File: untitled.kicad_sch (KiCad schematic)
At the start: 32 parts

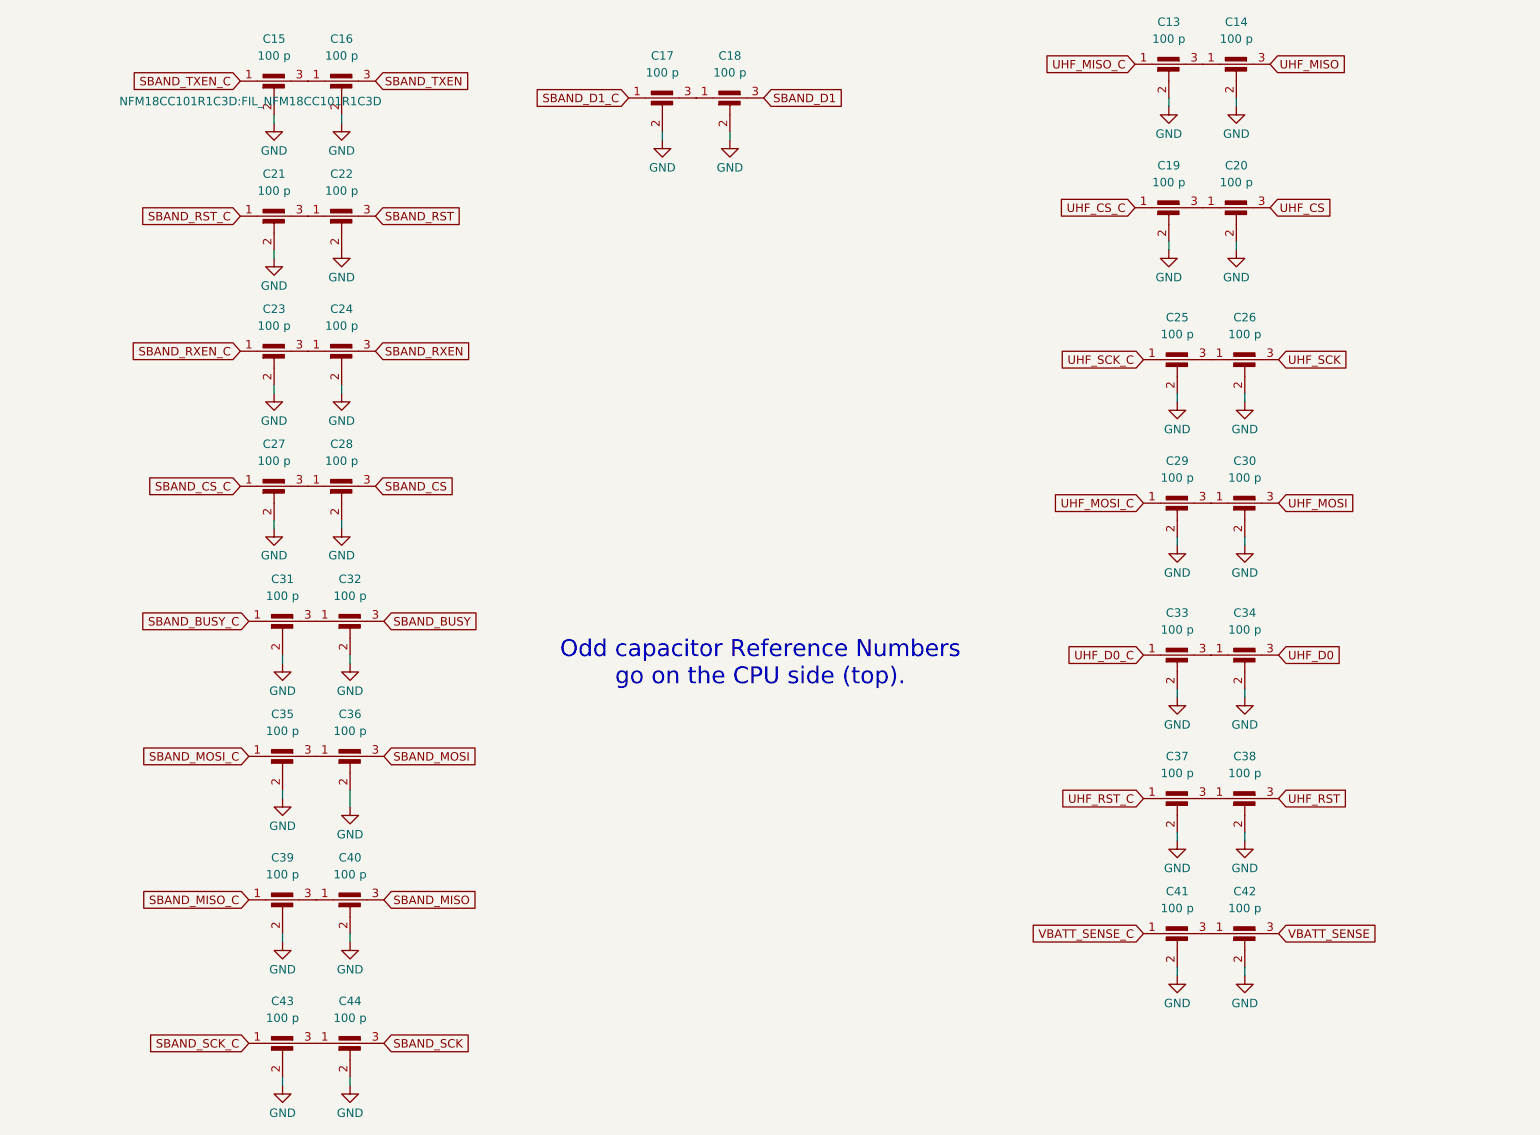
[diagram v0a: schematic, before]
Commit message: started placement of feed through
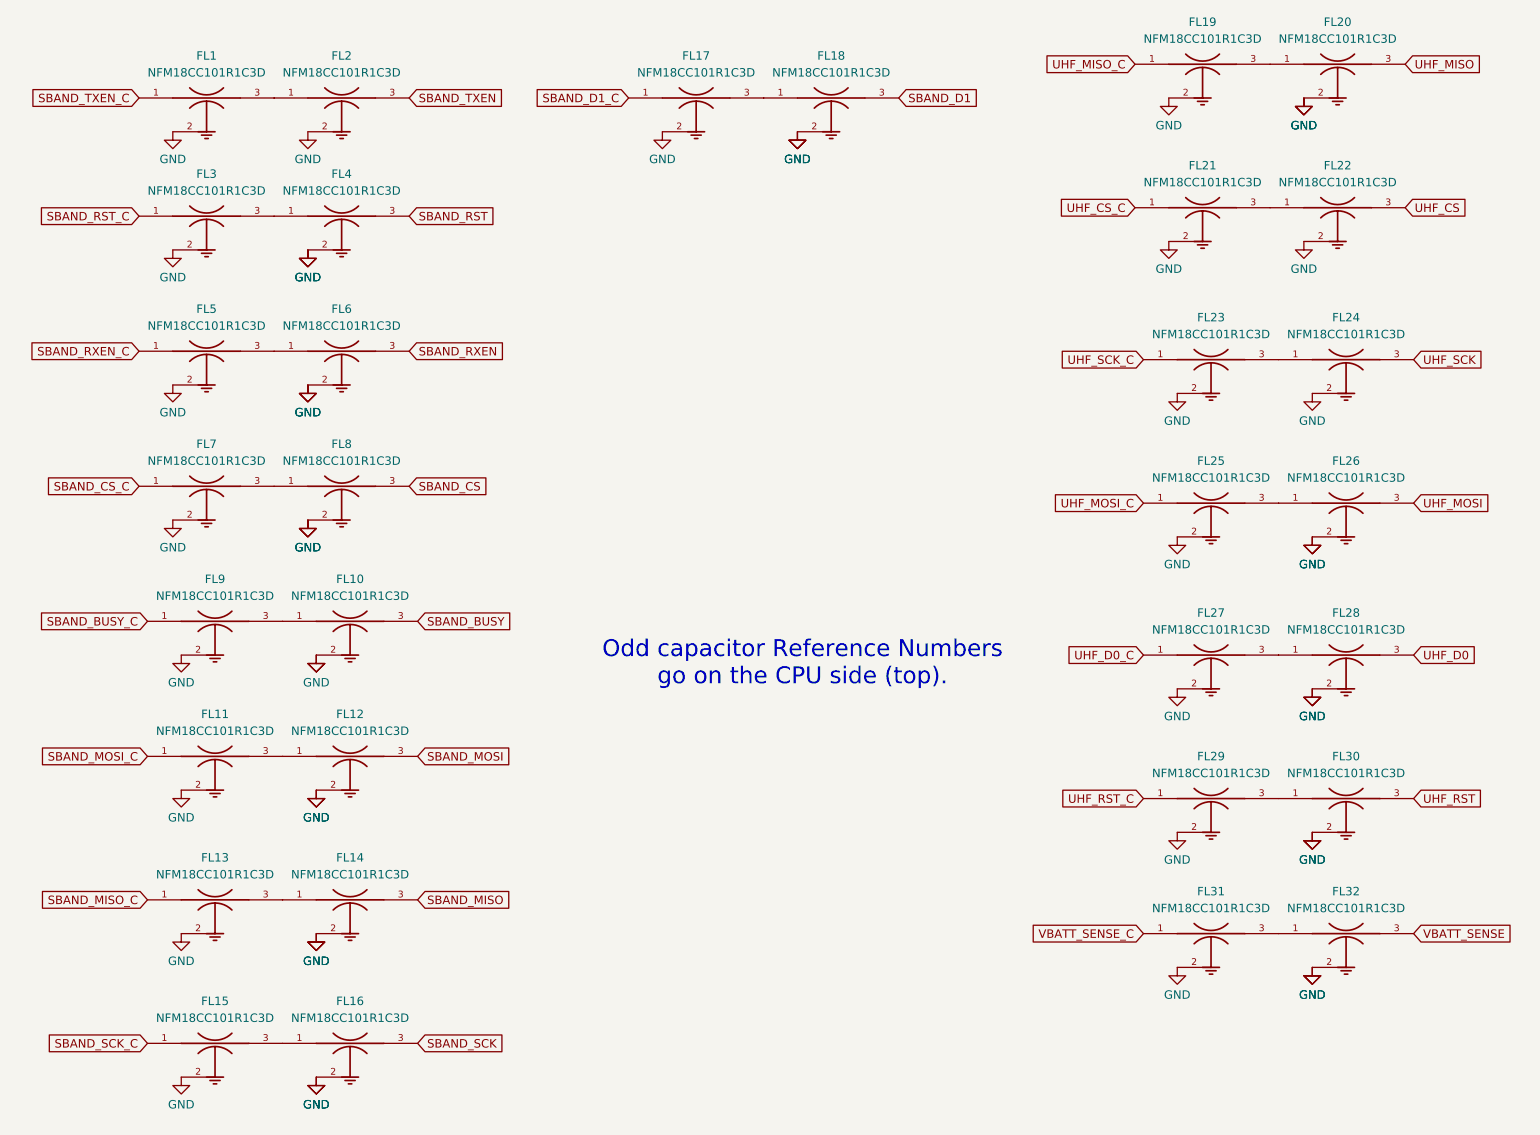
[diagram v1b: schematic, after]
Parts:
- removed C13, C14, C15, C16, C17, C18, C19, C20, C21, C22, C23, C24, C25, C26, C27, C28, C29, C30, C31, C32, C33, C34, C35, C36, C37, C38, C39, C40, C41, C42, C43, C44: 100 p, NFM18CC101R1C3D:FIL_NFM18CC101R1C3D, symbol Device:C_Feedthrough
- added FL1, FL10, FL11, FL12, FL13, FL14, FL15, FL16, FL17, FL18, FL19, FL2, FL20, FL21, FL22, FL23, FL24, FL25, FL26, FL27, FL28, FL29, FL3, FL30, FL31, FL32, FL4, FL5, FL6, FL7, FL8, FL9: NFM18CC101R1C3D, NFM18CC101R1C3D:FIL_NFM18CC101R1C3D, symbol NFM18CC101R1C3D:NFM18CC101R1C3D
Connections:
- net GND: now also FL1.2, FL1.2_1, FL1.2_2, FL1.2_3, FL1.2_4, FL10.2, FL10.2_1, FL10.2_2, FL10.2_3, FL10.2_4, FL11.2, FL11.2_1, FL11.2_2, FL11.2_3, FL11.2_4, FL12.2, FL12.2_1, FL12.2_2, FL12.2_3, FL12.2_4, FL13.2, FL13.2_1, FL13.2_2, FL13.2_3, FL13.2_4, FL14.2, FL14.2_1, FL14.2_2, FL14.2_3, FL14.2_4, FL15.2, FL15.2_1, FL15.2_2, FL15.2_3, FL15.2_4, FL16.2, FL16.2_1, FL16.2_2, FL16.2_3, FL16.2_4, FL17.2, FL17.2_1, FL17.2_2, FL17.2_3, FL17.2_4, FL18.2, FL18.2_1, FL18.2_2, FL18.2_3, FL18.2_4, FL19.2, FL19.2_1, FL19.2_2, FL19.2_3, FL19.2_4, FL2.2, FL2.2_1, FL2.2_2, FL2.2_3, FL2.2_4, FL20.2, FL20.2_1, FL20.2_2, FL20.2_3, FL20.2_4, FL21.2, FL21.2_1, FL21.2_2, FL21.2_3, FL21.2_4, FL22.2, FL22.2_1, FL22.2_2, FL22.2_3, FL22.2_4, FL23.2, FL23.2_1, FL23.2_2, FL23.2_3, FL23.2_4, FL24.2, FL24.2_1, FL24.2_2, FL24.2_3, FL24.2_4, FL25.2, FL25.2_1, FL25.2_2, FL25.2_3, FL25.2_4, FL26.2, FL26.2_1, FL26.2_2, FL26.2_3, FL26.2_4, FL27.2, FL27.2_1, FL27.2_2, FL27.2_3, FL27.2_4, FL28.2, FL28.2_1, FL28.2_2, FL28.2_3, FL28.2_4, FL29.2, FL29.2_1, FL29.2_2, FL29.2_3, FL29.2_4, FL3.2, FL3.2_1, FL3.2_2, FL3.2_3, FL3.2_4, FL30.2, FL30.2_1, FL30.2_2, FL30.2_3, FL30.2_4, FL31.2, FL31.2_1, FL31.2_2, FL31.2_3, FL31.2_4, FL32.2, FL32.2_1, FL32.2_2, FL32.2_3, FL32.2_4, FL4.2, FL4.2_1, FL4.2_2, FL4.2_3, FL4.2_4, FL5.2, FL5.2_1, FL5.2_2, FL5.2_3, FL5.2_4, FL6.2, FL6.2_1, FL6.2_2, FL6.2_3, FL6.2_4, FL7.2, FL7.2_1, FL7.2_2, FL7.2_3, FL7.2_4, FL8.2, FL8.2_1, FL8.2_2, FL8.2_3, FL8.2_4, FL9.2, FL9.2_1, FL9.2_2, FL9.2_3, FL9.2_4
- net SBAND_BUSY: now also FL10.3
- net SBAND_BUSY_C: now also FL9.1
- net SBAND_CS: now also FL8.3
- net SBAND_CS_C: now also FL7.1
- net SBAND_D1: now also FL18.3
- net SBAND_D1_C: now also FL17.1
- net SBAND_MISO: now also FL14.3
- net SBAND_MISO_C: now also FL13.1
- net SBAND_MOSI: now also FL12.3
- net SBAND_MOSI_C: now also FL11.1
- net SBAND_RST: now also FL4.3
- net SBAND_RST_C: now also FL3.1
- net SBAND_RXEN: now also FL6.3
- net SBAND_RXEN_C: now also FL5.1
- net SBAND_SCK: now also FL16.3
- net SBAND_SCK_C: now also FL15.1
- net SBAND_TXEN: now also FL2.3
- net SBAND_TXEN_C: now also FL1.1
- net UHF_CS: now also FL22.3
- net UHF_CS_C: now also FL21.1
- net UHF_D0: now also FL28.3
- net UHF_D0_C: now also FL27.1
- net UHF_MISO: now also FL20.3
- net UHF_MISO_C: now also FL19.1
- net UHF_MOSI: now also FL26.3
- net UHF_MOSI_C: now also FL25.1
- net UHF_RST: now also FL30.3
- net UHF_RST_C: now also FL29.1
- net UHF_SCK: now also FL24.3
- net UHF_SCK_C: now also FL23.1
- net VBATT_SENSE: now also FL32.3
- net VBATT_SENSE_C: now also FL31.1
- new net: FL19.3, FL20.1
- new net: FL27.3, FL28.1
- new net: FL25.3, FL26.1
- new net: FL21.3, FL22.1
- new net: FL5.3, FL6.1
- new net: FL7.3, FL8.1
- new net: FL23.3, FL24.1
- new net: FL10.1, FL9.3
- new net: FL1.3, FL2.1
- new net: FL15.3, FL16.1
- new net: FL3.3, FL4.1
- new net: FL17.3, FL18.1
- new net: FL29.3, FL30.1
- new net: FL11.3, FL12.1
- new net: FL31.3, FL32.1
- new net: FL13.3, FL14.1

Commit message: Power Monitor and 5V reg laid out; mechanicals on USER1 layer
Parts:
- removed FL32: NFM18CC101R1C3D, NFM18CC101R1C3D:FIL_NFM18CC101R1C3D, symbol NFM18CC101R1C3D:NFM18CC101R1C3D
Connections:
- net VBATT_SENSE: now also FL31.3
